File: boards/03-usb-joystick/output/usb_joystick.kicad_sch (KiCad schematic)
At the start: 19 parts, among them J1 TYPE-C, J2 Joystick, SW1 Button, SW2 Button, SW3 Button, SW4 Button, U1 MCU, Y1 16MHz

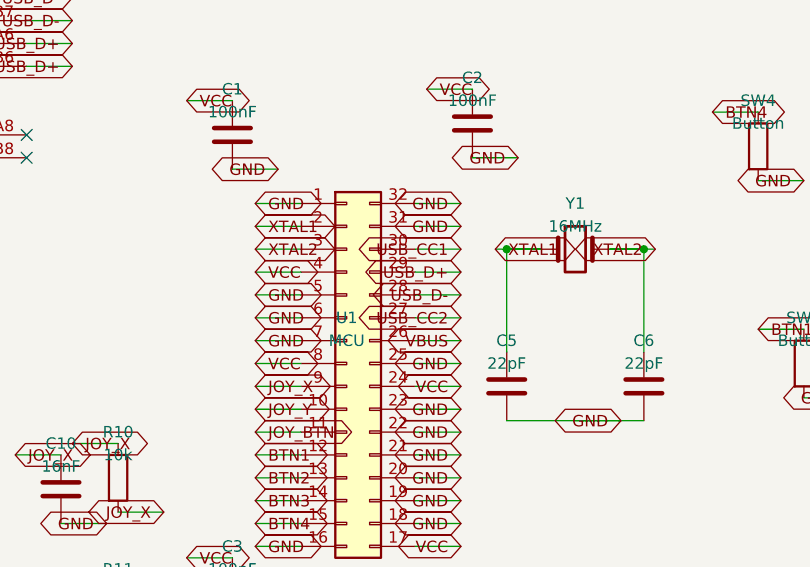
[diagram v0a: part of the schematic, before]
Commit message: feat(optim): rotate edge-constrained connectors to face off-board
An `EdgeConstraint` could only translate a component toward its board
edge. A USB-C receptacle could therefore sit flush at the perimeter with
its plug opening aimed at the board interior -- placement the
EDGE_CONNECTOR_PLACEMENT check accepts but no cable can mate with. That
is exactly how board-03's J1 shipped: 7.6 mm inboard of the north edge,
mouth pointing at the buttons.

Library capability:

- `EdgeConstraint.mating_face_offset_deg` -- the off-board direction of a
  footprint's mating face in its own 0-degree frame (KiCad board frame,
  +Y = south). `None` keeps the pre-existing translation-only behavior.
- `compute_edge_orientation_torque()` -- torsion spring toward alignment
  with the assigned edge's outward `Edge.normal()`, summed into
  `PlacementOptimizer.compute_forces_and_torques()` alongside the
  existing 90-degree rotation-potential torque. Its magnitude saturates
  past 90 degrees of misalignment so the 180-degree (mouth-inward) case
  is not a zero-torque saddle.
- `edge_orientation_potential_energy()` -- added to `compute_energy()`,
  without which `run()` calls convergence (it samples linear velocity
  only) while a connector is still mid-flip.
- `snap_rotations()` resolves a hinted edge connector to the grid slot
  that faces off-board instead of the nearest one; the board boundary's
  own alignment torque has equal wells 180 degrees apart, so the discrete
  step is where the requirement has to be settled deterministically.
- `detect_edge_components(mating_faces=...)` / `from_pcb(mating_faces=...)`
  thread caller-supplied per-reference hints through.

board-03 consumes it:

- J1 rotated 180 degrees so the plug opening faces off the north edge,
  seated 0.5 mm inside Edge.Cuts, and given F.CrtYd artwork covering the
  real receptacle body -- without it the footprint claims to be only its
  pad field and the 7.4 mm body is invisible to every checker.
- U1's north-edge USB pins re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
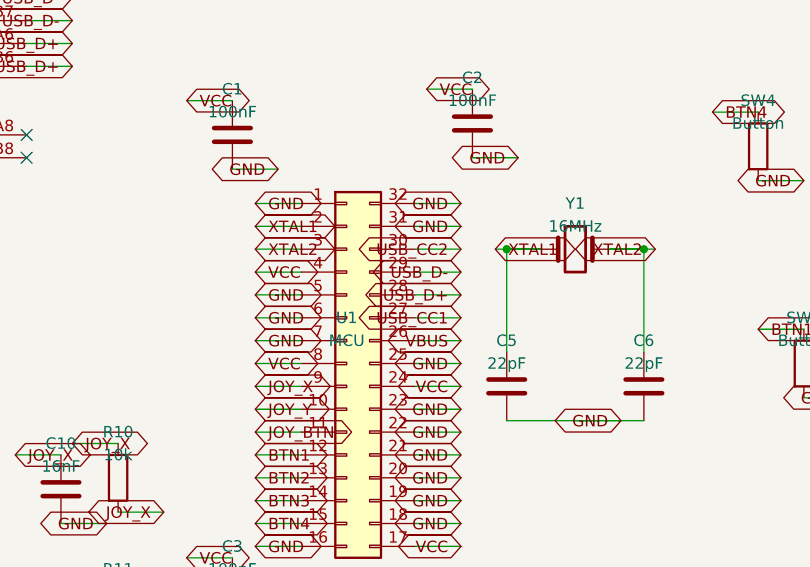
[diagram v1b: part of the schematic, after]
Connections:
- net USB_CC1: now also U1.27 (Pin_27); no longer U1.30 (Pin_30)
- net USB_CC2: now also U1.30 (Pin_30); no longer U1.27 (Pin_27)
- net USB_D+: now also U1.28 (Pin_28); no longer U1.29 (Pin_29)
- net USB_D-: now also U1.29 (Pin_29); no longer U1.28 (Pin_28)
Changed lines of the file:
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@@
 	(version 20231120)
 	(generator "eeschema")
-	(generator_version "9.0")
+	(generator_version "10.0")
 	(paper "A4")
 	(title_block
@@
 		(instances
 			(project "project"
-				(path "/05987b2f-1bb3-4148-8126-f02f0f3f6b9c" (reference "U1") (unit 1)
+				(path "/3e933430-7aee-490f-b368-bae26cc54027" (reference "U1") (unit 1)
 				)
 			)
@@
 		(instances
 			(project "project"
-				(path "/05987b2f-1bb3-4148-8126-f02f0f3f6b9c" (reference "J1") (unit 1)
+				(path "/3e933430-7aee-490f-b368-bae26cc54027" (reference "J1") (unit 1)
 				)
 			)
@@
 		(instances
 			(project "project"
-				(path "/05987b2f-1bb3-4148-8126-f02f0f3f6b9c" (reference "J2") (unit 1)
+				(path "/3e933430-7aee-490f-b368-bae26cc54027" (reference "J2") (unit 1)
 				)
 			)
@@
 		(instances
 			(project "project"
-				(path "/05987b2f-1bb3-4148-8126-f02f0f3f6b9c" (reference "R10") (unit 1)
+				(path "/3e933430-7aee-490f-b368-bae26cc54027" (reference "R10") (unit 1)
 				)
 			)
@@
 		(instances
 			(project "project"
-				(path "/05987b2f-1bb3-4148-8126-f02f0f3f6b9c" (reference "C10") (unit 1)
+				(path "/3e933430-7aee-490f-b368-bae26cc54027" (reference "C10") (unit 1)
 				)
 			)
@@
 		(instances
 			(project "project"
-				(path "/05987b2f-1bb3-4148-8126-f02f0f3f6b9c" (reference "R11") (unit 1)
+				(path "/3e933430-7aee-490f-b368-bae26cc54027" (reference "R11") (unit 1)
 				)
 			)
@@
 		(instances
 			(project "project"
-				(path "/05987b2f-1bb3-4148-8126-f02f0f3f6b9c" (reference "C11") (unit 1)
+				(path "/3e933430-7aee-490f-b368-bae26cc54027" (reference "C11") (unit 1)
 				)
 			)
@@
 		(instances
 			(project "project"
-				(path "/05987b2f-1bb3-4148-8126-f02f0f3f6b9c" (reference "R12") (unit 1)
+				(path "/3e933430-7aee-490f-b368-bae26cc54027" (reference "R12") (unit 1)
 				)
 			)
@@
 		(instances
 			(project "project"
-				(path "/05987b2f-1bb3-4148-8126-f02f0f3f6b9c" (reference "Y1") (unit 1)
+				(path "/3e933430-7aee-490f-b368-bae26cc54027" (reference "Y1") (unit 1)
 				)
 			)
@@
 		(instances
 			(project "project"
-				(path "/05987b2f-1bb3-4148-8126-f02f0f3f6b9c" (reference "C5") (unit 1)
+				(path "/3e933430-7aee-490f-b368-bae26cc54027" (reference "C5") (unit 1)
 				)
 			)
@@
 		(instances
 			(project "project"
-				(path "/05987b2f-1bb3-4148-8126-f02f0f3f6b9c" (reference "C6") (unit 1)
+				(path "/3e933430-7aee-490f-b368-bae26cc54027" (reference "C6") (unit 1)
 				)
 			)
@@
 		(instances
 			(project "project"
-				(path "/05987b2f-1bb3-4148-8126-f02f0f3f6b9c" (reference "SW1") (unit 1)
+				(path "/3e933430-7aee-490f-b368-bae26cc54027" (reference "SW1") (unit 1)
 				)
 			)
@@
 		(instances
 			(project "project"
-				(path "/05987b2f-1bb3-4148-8126-f02f0f3f6b9c" (reference "SW2") (unit 1)
+				(path "/3e933430-7aee-490f-b368-bae26cc54027" (reference "SW2") (unit 1)
 				)
 			)
@@
 		(instances
 			(project "project"
-				(path "/05987b2f-1bb3-4148-8126-f02f0f3f6b9c" (reference "SW3") (unit 1)
+				(path "/3e933430-7aee-490f-b368-bae26cc54027" (reference "SW3") (unit 1)
 				)
 			)
@@
 		(instances
 			(project "project"
-				(path "/05987b2f-1bb3-4148-8126-f02f0f3f6b9c" (reference "SW4") (unit 1)
+				(path "/3e933430-7aee-490f-b368-bae26cc54027" (reference "SW4") (unit 1)
 				)
 			)
@@
 		(instances
 			(project "project"
-				(path "/05987b2f-1bb3-4148-8126-f02f0f3f6b9c" (reference "C1") (unit 1)
+				(path "/3e933430-7aee-490f-b368-bae26cc54027" (reference "C1") (unit 1)
 				)
 			)
@@
 		(instances
 			(project "project"
-				(path "/05987b2f-1bb3-4148-8126-f02f0f3f6b9c" (reference "C2") (unit 1)
+				(path "/3e933430-7aee-490f-b368-bae26cc54027" (reference "C2") (unit 1)
 				)
 			)
@@
 		(instances
 			(project "project"
-				(path "/05987b2f-1bb3-4148-8126-f02f0f3f6b9c" (reference "C3") (unit 1)
+				(path "/3e933430-7aee-490f-b368-bae26cc54027" (reference "C3") (unit 1)
 				)
 			)
@@
 		(instances
 			(project "project"
-				(path "/05987b2f-1bb3-4148-8126-f02f0f3f6b9c" (reference "C4") (unit 1)
+				(path "/3e933430-7aee-490f-b368-bae26cc54027" (reference "C4") (unit 1)
 				)
 			)
@@
 		(instances
 			(project "project"
-				(path "/05987b2f-1bb3-4148-8126-f02f0f3f6b9c" (reference "#PWR01") (unit 1)
+				(path "/3e933430-7aee-490f-b368-bae26cc54027" (reference "#PWR01") (unit 1)
 				)
 			)
@@
 		(instances
 			(project "project"
-				(path "/05987b2f-1bb3-4148-8126-f02f0f3f6b9c" (reference "#PWR02") (unit 1)
+				(path "/3e933430-7aee-490f-b368-bae26cc54027" (reference "#PWR02") (unit 1)
 				)
 			)
@@
 		(instances
 			(project "project"
-				(path "/05987b2f-1bb3-4148-8126-f02f0f3f6b9c" (reference "#PWR03") (unit 1)
+				(path "/3e933430-7aee-490f-b368-bae26cc54027" (reference "#PWR03") (unit 1)
 				)
 			)
@@
 		(instances
 			(project "project"
-				(path "/05987b2f-1bb3-4148-8126-f02f0f3f6b9c" (reference "#PWR04") (unit 1)
+				(path "/3e933430-7aee-490f-b368-bae26cc54027" (reference "#PWR04") (unit 1)
 				)
 			)
@@
 		)
 	)
-	(global_label "USB_CC2" (shape bidirectional) (at 114.3 83.82 180) (fields_autoplaced yes)
-		(effects
-			(font
-				(size 1.27 1.27)
-			)
-			(justify right)
-		)
-	)
-	(global_label "USB_D-" (shape bidirectional) (at 114.3 81.28 180) (fields_autoplaced yes)
-		(effects
-			(font
-				(size 1.27 1.27)
-			)
-			(justify right)
-		)
-	)
-	(global_label "USB_D+" (shape bidirectional) (at 114.3 78.74 180) (fields_autoplaced yes)
-		(effects
-			(font
-				(size 1.27 1.27)
-			)
-			(justify right)
-		)
-	)
-	(global_label "USB_CC1" (shape bidirectional) (at 114.3 76.2 180) (fields_autoplaced yes)
+	(global_label "USB_CC1" (shape bidirectional) (at 114.3 83.82 180) (fields_autoplaced yes)
+		(effects
+			(font
+				(size 1.27 1.27)
+			)
+			(justify right)
+		)
+	)
+	(global_label "USB_D+" (shape bidirectional) (at 114.3 81.28 180) (fields_autoplaced yes)
+		(effects
+			(font
+				(size 1.27 1.27)
+			)
+			(justify right)
+		)
+	)
+	(global_label "USB_D-" (shape bidirectional) (at 114.3 78.74 180) (fields_autoplaced yes)
+		(effects
+			(font
+				(size 1.27 1.27)
+			)
+			(justify right)
+		)
+	)
+	(global_label "USB_CC2" (shape bidirectional) (at 114.3 76.2 180) (fields_autoplaced yes)
 		(effects
 			(font
@@
 	)
 	(sheet_instances
-		(path "/05987b2f-1bb3-4148-8126-f02f0f3f6b9c" (page "1")
-		)
-	)
+		(path "/3e933430-7aee-490f-b368-bae26cc54027" (page "1")
+		)
+	)
